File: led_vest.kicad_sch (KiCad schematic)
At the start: 8 parts, among them J1 Conn_01x02_Socket, U1 PTPS61288RQQR, U2 ATtiny1616-S

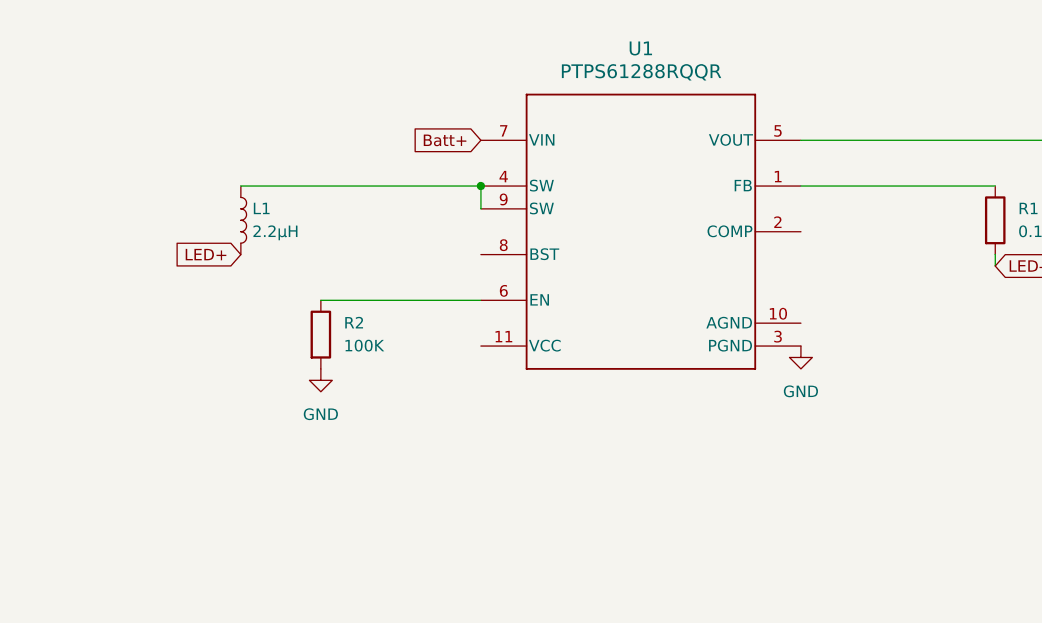
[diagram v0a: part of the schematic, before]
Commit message: fix boost converter
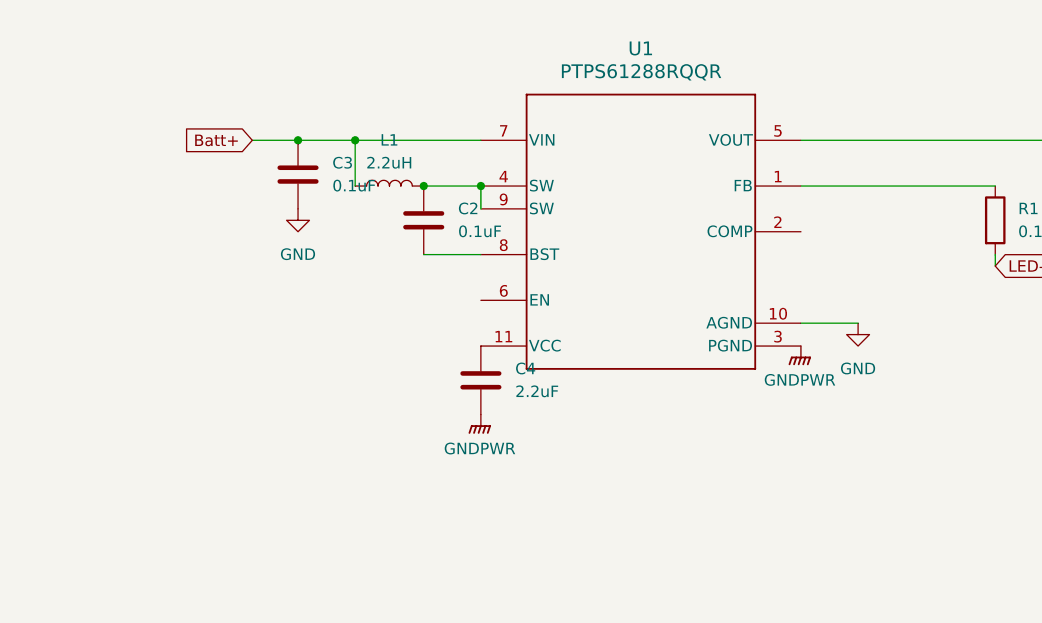
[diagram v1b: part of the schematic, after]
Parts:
- removed R2: 100K, symbol Device:R
- added C2, C3: 0.1uF, symbol Device:C
- added C4: 2.2uF, symbol Device:C
- L1: value 2.2µH -> 2.2uH
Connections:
- net Batt+: now also L1.1, C3.1
- net GND: now also U1.10 (AGND), C3.2; no longer U1.3 (PGND)
- net LED+: no longer L1.2
- net at U1.11 (VCC): now also C4.1
- net at U1.4 (SW), U1.9 (SW): now also L1.2, C2.1; no longer L1.1
- net at U1.8 (BST): now also C2.2
- new net GNDPWR: C4.2, U1.3 (PGND)
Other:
- moved on the sheet: L1

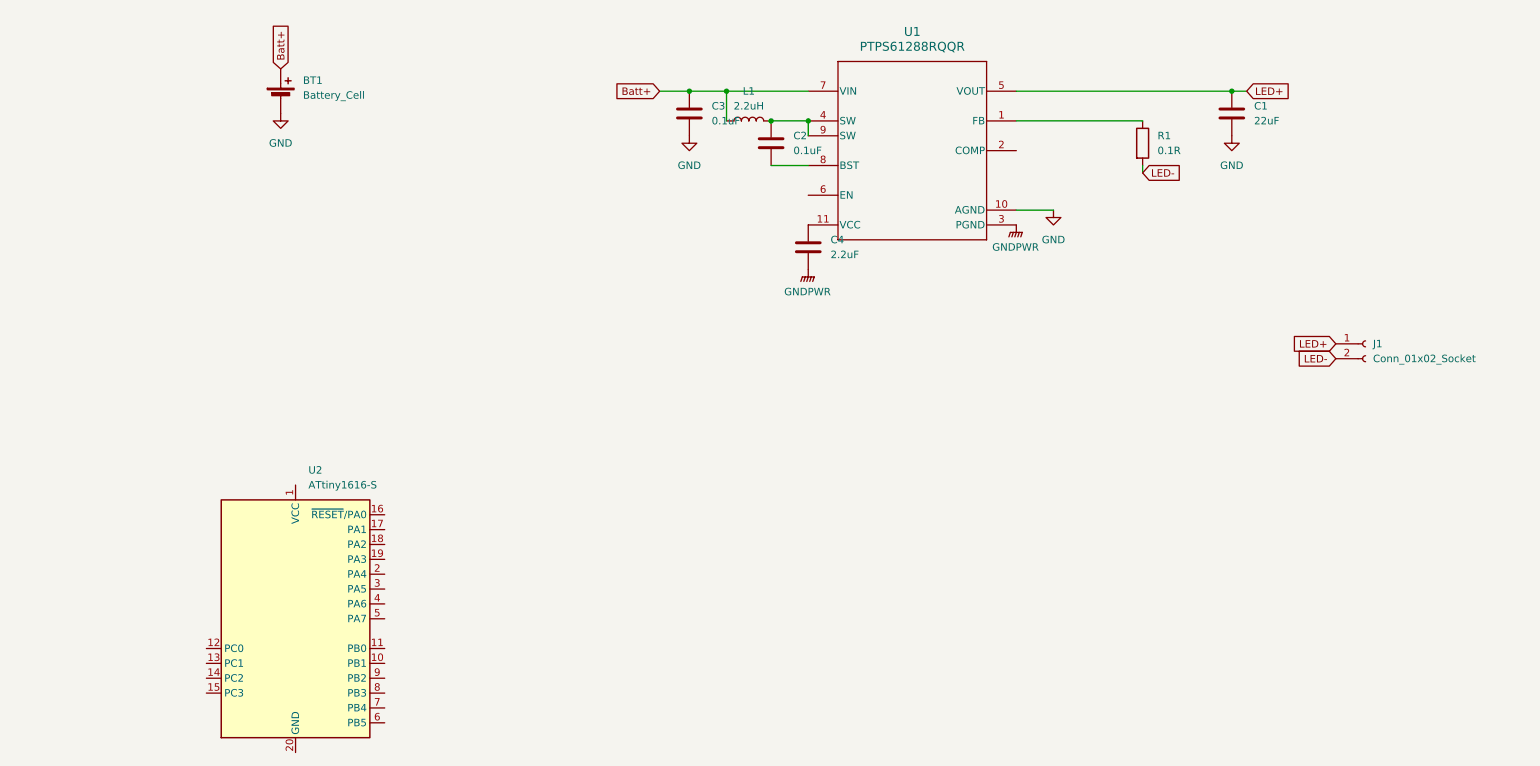
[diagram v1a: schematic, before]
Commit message: all components in schematic
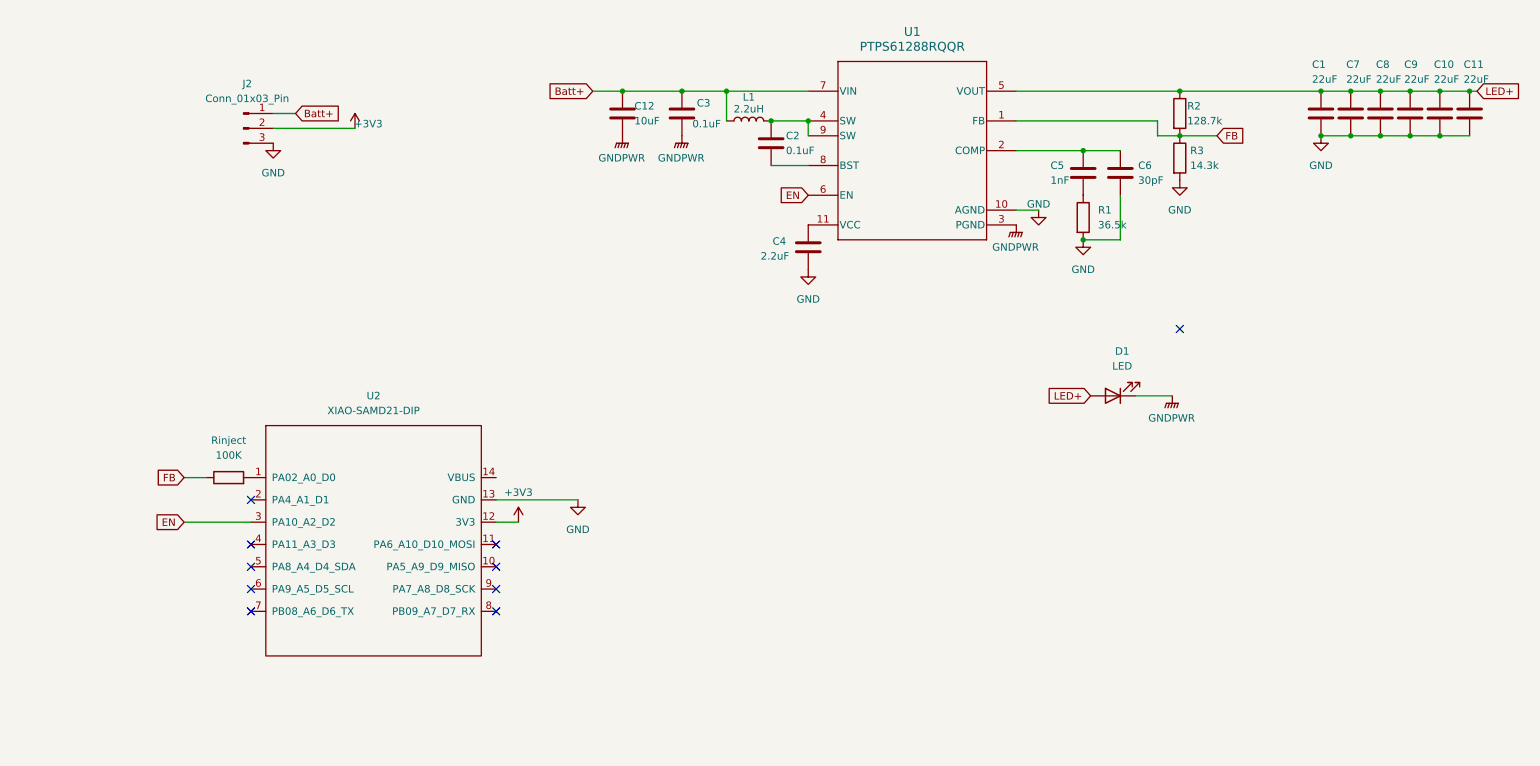
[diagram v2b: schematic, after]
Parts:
- removed BT1: Battery_Cell, symbol Device:Battery_Cell
- removed J1: Conn_01x02_Socket, symbol Connector:Conn_01x02_Socket
- removed U2: ATtiny1616-S, Package_SO:SOIC-20W_7.5x12.8mm_P1.27mm, symbol MCU_Microchip_ATtiny:ATtiny1616-S
- added C10, C11, C7, C8, C9: 22uF, symbol Device:C
- added C12: 10uF, symbol Device:C
- added C5: 1nF, symbol Device:C
- added C6: 30pF, symbol Device:C
- added D1: LED, symbol Device:LED
- added J2: Conn_01x03_Pin, symbol Connector:Conn_01x03_Pin
- added R2: 128.7k, symbol Device:R
- added R3: 14.3k, symbol Device:R
- added Rinject: 100K, symbol Device:R
- added U2: XIAO-SAMD21-DIP, Seeed_Studio_XIAO_Series:XIAO-SAMD21-DIP, symbol Seeed_Studio_XIAO_Series:XIAO-SAMD21-DIP
- R1: value 0.1R -> 36.5k
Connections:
- net LED- is gone; now on net GND: R1.2
- net Batt+: now also C12.1, J2.1 (Pin_1)
- net GND: now also C4.2, C10.2, C11.2, C6.2, C7.2, C8.2, C9.2, J2.3 (Pin_3), R3.2, U2.13 (GND); no longer C3.2
- net GNDPWR: now also C3.2, C12.2, D1.1 (K); no longer C4.2
- net LED+: now also C10.1, C11.1, C7.1, C8.1, C9.1, D1.2 (A), R2.1
- net at R1.1: now also C5.2; no longer U1.1 (FB)
- net at U1.2 (COMP): now also C5.1, C6.1
- net EN: now reaches U1.6 (EN)
- net EN: now also U2.3 (PA10_A2_D2)
- new net: Rinject.2, U2.1 (PA02_A0_D0)
- new net +3V3: J2.2 (Pin_2), U2.12 (3V3)
- new net FB: R2.2, R3.1, Rinject.1, U1.1 (FB)
- no-connect marks 0 -> 10
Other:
- moved on the sheet: C1, C3

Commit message: add current sensing circuit
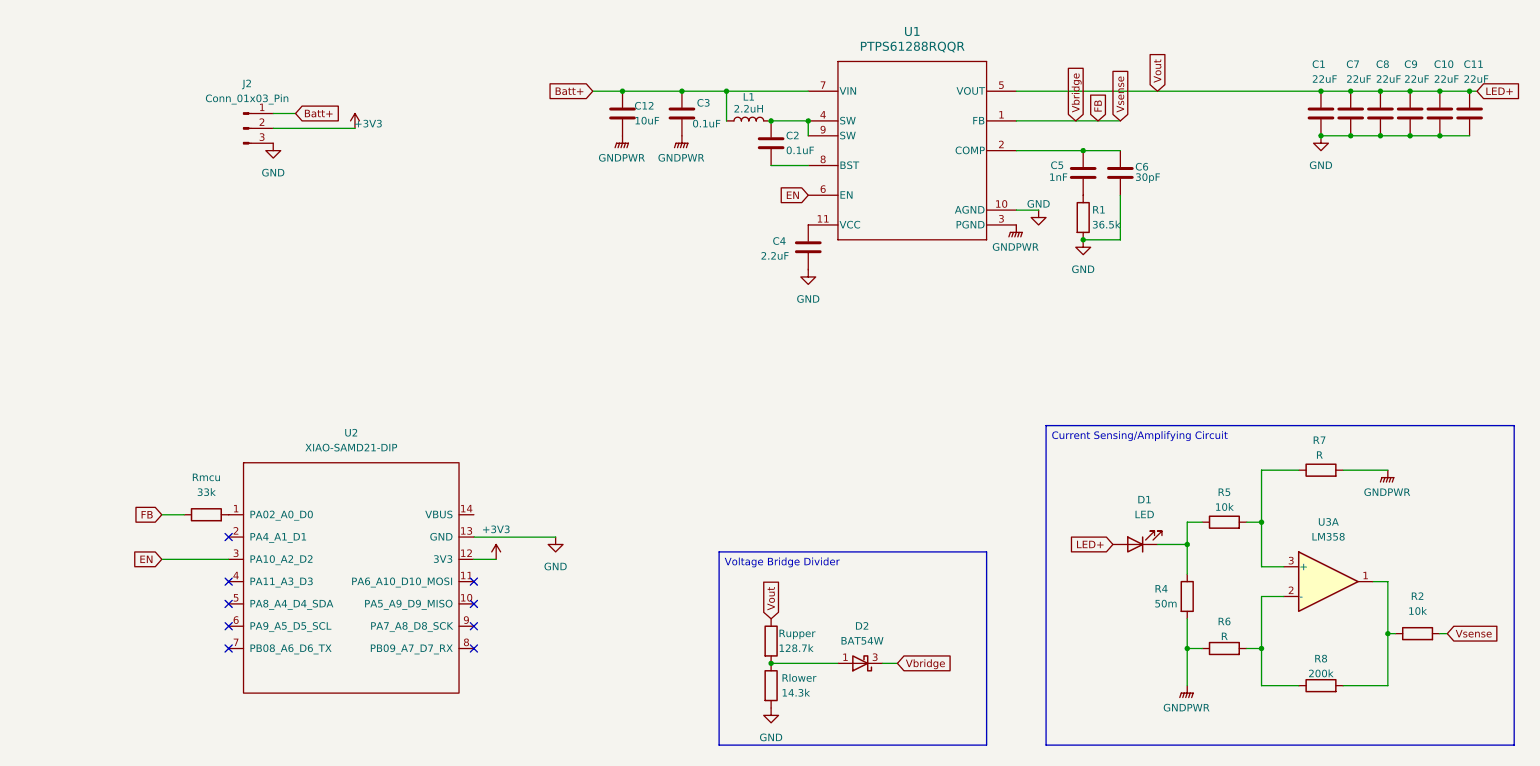
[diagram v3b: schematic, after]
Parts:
- added D2: BAT54W, Package_TO_SOT_SMD:SOT-323_SC-70, symbol Diode:BAT54W
- added R2, R5: 10k, symbol Device:R
- added R4: 50m, symbol Device:R
- added R6, R7: R, symbol Device:R
- added R8: 200k, symbol Device:R
- added U3: LM358, symbol Amplifier_Operational:LM358
- Rmcu: renamed from Rinject; value 100K -> 33k
- renumbered R3 to Rlower, R2 to Rupper
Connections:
- net FB: now also D2.3 (K), R2.2; no longer Rlower.1, Rupper.2
- net GNDPWR: now also R4.2, R6.1, R7.2; no longer D1.1 (K)
- new net: D1.1 (K), R4.1, R5.1
- new net: R6.2, R8.1, U3.2 (-)
- new net: D2.1 (A), Rlower.1, Rupper.2
- new net: R2.1, R8.2, U3.1
- new net: R5.2, R7.1, U3.3 (+)
- no-connect marks 10 -> 9
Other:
- moved on the sheet: D1, Rlower, Rmcu, Rupper, U2

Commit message: add button to IO pin
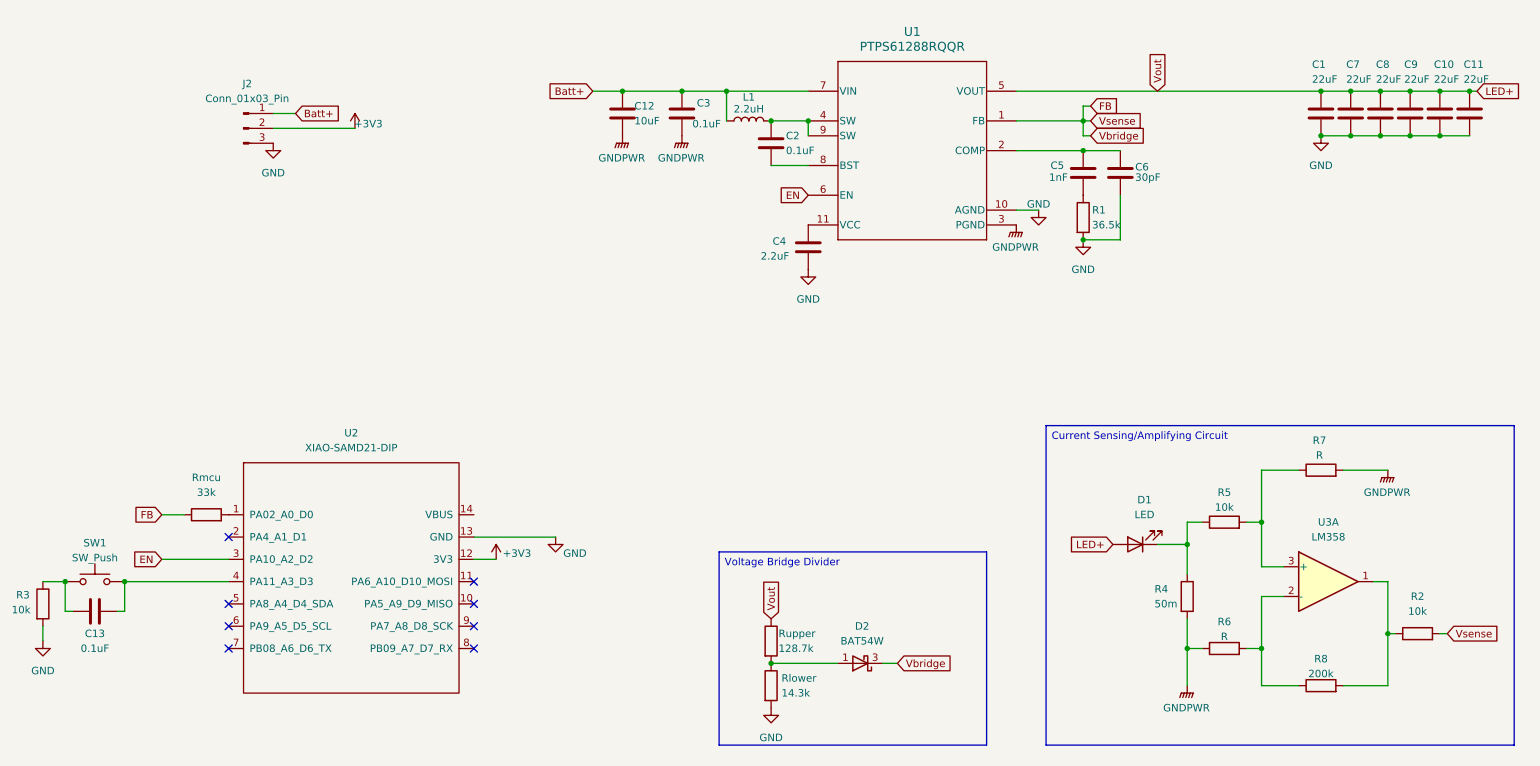
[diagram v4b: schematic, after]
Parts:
- added C13: 0.1uF, symbol Device:C
- added R3: 10k, symbol Device:R
- added SW1: SW_Push, symbol Switch:SW_Push
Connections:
- net GND: now also R3.2
- net at U2.4 (PA11_A3_D3): now also C13.2, SW1.2
- new net: C13.1, R3.1, SW1.1
- no-connect marks 9 -> 8

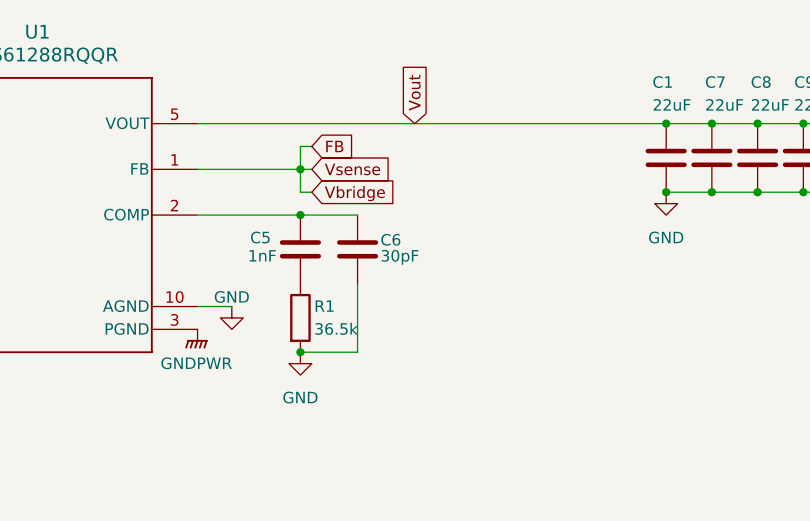
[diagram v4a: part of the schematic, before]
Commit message: add capacitor on FB pin to ground
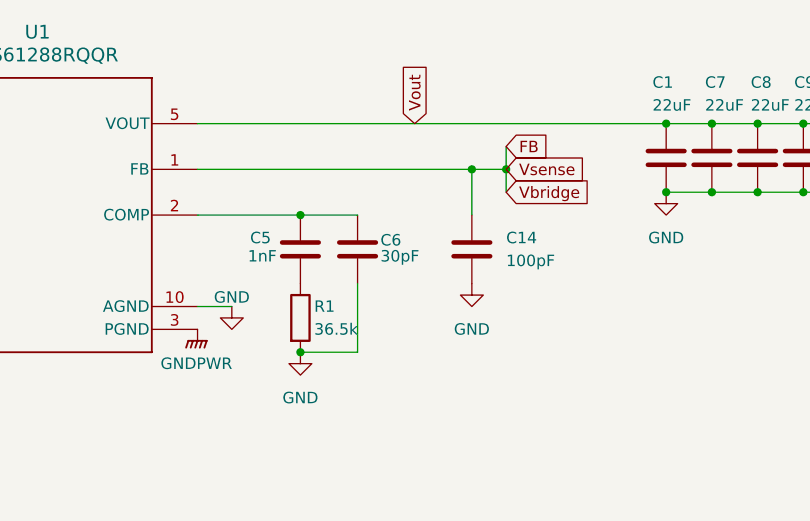
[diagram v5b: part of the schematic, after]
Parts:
- added C14: 100pF, symbol Device:C
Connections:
- net FB: now also C14.1
- net GND: now also C14.2
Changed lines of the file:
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@@
 	)
 	(junction
-		(at 241.3 45.72)
+		(at 223.52 50.8)
 		(diameter 0)
 		(color 0 0 0 0)
 	)
 	(junction
-		(at 241.3 53.34)
+		(at 241.3 45.72)
 		(diameter 0)
 		(color 0 0 0 0)
 	)
 	(junction
-		(at 147.32 50.8)
+		(at 241.3 53.34)
 		(diameter 0)
 		(color 0 0 0 0)
 	)
 	(junction
-		(at 231.14 140.97)
+		(at 147.32 50.8)
 		(diameter 0)
 		(color 0 0 0 0)
 	)
 	(junction
-		(at 200.66 50.8)
+		(at 231.14 140.97)
 		(diameter 0)
 		(color 0 0 0 0)
@@
 	)
 	(junction
+		(at 219.71 50.8)
+		(diameter 0)
+		(color 0 0 0 0)
+	)
+	(junction
 		(at 139.7 45.72)
 		(diameter 0)
@@
 	(wire
 		(pts
-			(xy 189.23 50.8) (xy 200.66 50.8)
-		)
-		(stroke
-			(width 0)
-			(type default)
-		)
-	)
-	(wire
-		(pts
-			(xy 200.66 53.34) (xy 200.66 50.8)
+			(xy 223.52 53.34) (xy 223.52 50.8)
 		)
 		(stroke
@@
 	(wire
 		(pts
-			(xy 218.44 135.89) (xy 218.44 140.97)
+			(xy 219.71 50.8) (xy 223.52 50.8)
 		)
 		(stroke
@@
 	(wire
 		(pts
-			(xy 96.52 121.92) (xy 110.49 121.92)
+			(xy 218.44 135.89) (xy 218.44 140.97)
 		)
 		(stroke
@@
 	(wire
 		(pts
-			(xy 200.66 50.8) (xy 201.93 50.8)
+			(xy 96.52 121.92) (xy 110.49 121.92)
 		)
 		(stroke
@@
 	(wire
 		(pts
-			(xy 201.93 48.26) (xy 200.66 48.26)
-		)
-		(stroke
-			(width 0)
-			(type default)
-		)
-	)
-	(wire
-		(pts
 			(xy 189.23 66.04) (xy 193.04 66.04)
 		)
@@
 	(wire
 		(pts
-			(xy 200.66 48.26) (xy 200.66 50.8)
+			(xy 223.52 48.26) (xy 223.52 50.8)
 		)
 		(stroke
@@
 	(wire
 		(pts
-			(xy 201.93 53.34) (xy 200.66 53.34)
+			(xy 36.83 129.54) (xy 54.61 129.54)
 		)
 		(stroke
@@
 	(wire
 		(pts
-			(xy 36.83 129.54) (xy 54.61 129.54)
+			(xy 189.23 45.72) (xy 241.3 45.72)
 		)
 		(stroke
@@
 	(wire
 		(pts
-			(xy 189.23 45.72) (xy 241.3 45.72)
+			(xy 35.56 134.62) (xy 36.83 134.62)
 		)
 		(stroke
@@
 	(wire
 		(pts
-			(xy 35.56 134.62) (xy 36.83 134.62)
+			(xy 261.62 138.43) (xy 262.89 138.43)
 		)
 		(stroke
@@
 	(wire
 		(pts
-			(xy 261.62 138.43) (xy 262.89 138.43)
+			(xy 189.23 50.8) (xy 219.71 50.8)
 		)
 		(stroke
@@
 	(wire
 		(pts
+			(xy 219.71 50.8) (xy 219.71 55.88)
+		)
+		(stroke
+			(width 0)
+			(type default)
+		)
+	)
+	(wire
+		(pts
 			(xy 252.73 138.43) (xy 252.73 147.32)
 		)
@@
 	(global_label "Vsense"
 		(shape input)
-		(at 201.93 50.8 0)
+		(at 223.52 50.8 0)
 		(fields_autoplaced yes)
 		(effects
@@
 		)
 		(property "Intersheetrefs" "${INTERSHEET_REFS}"
-			(at 211.3862 50.8 0)
+			(at 232.9762 50.8 0)
 			(effects
 				(font
@@
 	(global_label "Vbridge"
 		(shape input)
-		(at 201.93 53.34 0)
+		(at 223.52 53.34 0)
 		(fields_autoplaced yes)
 		(effects
@@
 		)
 		(property "Intersheetrefs" "${INTERSHEET_REFS}"
-			(at 211.9304 53.34 0)
+			(at 233.5204 53.34 0)
 			(effects
 				(font
@@
 	(global_label "FB"
 		(shape input)
-		(at 201.93 48.26 0)
+		(at 223.52 48.26 0)
 		(fields_autoplaced yes)
 		(effects
@@
 		)
 		(property "Intersheetrefs" "${INTERSHEET_REFS}"
-			(at 207.2738 48.26 0)
+			(at 228.8638 48.26 0)
 			(effects
 				(font
@@
 	)
 	(symbol
+		(lib_id "Device:C")
+		(at 219.71 59.69 0)
+		(unit 1)
+		(exclude_from_sim no)
+		(in_bom yes)
+		(on_board yes)
+		(dnp no)
+		(fields_autoplaced yes)
+		(property "Reference" "C14"
+			(at 223.52 58.4199 0)
+			(effects
+				(font
+					(size 1.27 1.27)
+				)
+				(justify left)
+			)
+		)
+		(property "Value" "100pF"
+			(at 223.52 60.9599 0)
+			(effects
+				(font
+					(size 1.27 1.27)
+				)
+				(justify left)
+			)
+		)
+		(property "Footprint" ""
+			(at 220.6752 63.5 0)
+			(effects
+				(font
+					(size 1.27 1.27)
+				)
+				(hide yes)
+			)
+		)
+		(property "Datasheet" "~"
+			(at 219.71 59.69 0)
+			(effects
+				(font
+					(size 1.27 1.27)
+				)
+				(hide yes)
+			)
+		)
+		(property "Description" "Unpolarized capacitor"
+			(at 219.71 59.69 0)
+			(effects
+				(font
+					(size 1.27 1.27)
+				)
+				(hide yes)
+			)
+		)
+		(pin "2"
+		)
+		(pin "1"
+		)
+		(instances
+			(project ""
+				(path "/d4f7e68f-7ec8-438b-89ce-97ee4db6cddd"
+					(reference "C14")
+					(unit 1)
+				)
+			)
+		)
+	)
+	(symbol
 		(lib_id "Device:R")
 		(at 147.32 139.7 0)
@@
 					(unit 1)
 				)
+			)
+		)
+	)
+	(symbol
+		(lib_id "power:GND")
+		(at 219.71 63.5 0)
+		(unit 1)
+		(exclude_from_sim no)
+		(in_bom yes)
+		(on_board yes)
+		(dnp no)
+		(fields_autoplaced yes)
+		(property "Reference" "#PWR016"
+			(at 219.71 69.85 0)
+			(effects
+				(font
+					(size 1.27 1.27)
+				)
+				(hide yes)
+			)
+		)
+		(property "Value" "GND"
+			(at 219.71 68.58 0)
+			(effects
+				(font
+					(size 1.27 1.27)
+				)
+			)
+		)
+		(property "Footprint" ""
+			(at 219.71 63.5 0)
+			(effects
+				(font
+					(size 1.27 1.27)
+				)
+				(hide yes)
+			)
+		)
+		(property "Datasheet" ""
+			(at 219.71 63.5 0)
+			(effects
+				(font
+					(size 1.27 1.27)
+				)
+				(hide yes)
+			)
+		)
+		(property "Description" "Power symbol creates a global label with name \"GND\" , ground"
+			(at 219.71 63.5 0)
+			(effects
+				(font
+					(size 1.27 1.27)
+				)
+				(hide yes)
+			)
+		)
+		(pin "1"
+		)
+		(instances
+			(project ""
+				(path "/d4f7e68f-7ec8-438b-89ce-97ee4db6cddd"
+					(reference "#PWR016")
+					(unit 1)
+				)
